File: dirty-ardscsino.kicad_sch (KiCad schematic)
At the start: 13 parts, among them J1 SCSI, J2 171825-4 (Ext. Power), J3 DM3AT-SF-PEJM5, U1 STM32 Bluepill

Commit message: Dirty ArdSCSIno 2 v1 sent to fab
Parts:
- removed JP2, JP3: Jumper_NC_Small, Connector_PinHeader_2.54mm:PinHeader_1x02_P2.54mm_Vertical, symbol Jumper:Jumper_2_Bridged
- added JP4, JP5: Jumper_2_Small_Bridged, Jumper:SolderJumper-2_P1.3mm_Bridged_RoundedPad1.0x1.5mm, symbol Jumper:Jumper_2_Small_Bridged
- added U2: microSD-Breakout, microSD_Breakout:microSD_AliExpress, symbol microSD_Breakout:microSD-Breakout
- C2: footprint Capacitor_SMD:C_0805_2012Metric_Pad1.15x1.40mm_HandSolder -> Capacitor_SMD:C_0805_2012Metric_Pad1.18x1.45mm_HandSolder
- JP1: value Jumper_NC_Small -> TERM_PWR_EN
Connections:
- net +5V: now also C2.2, RN1.1 (common), RN4.1 (common)
- net GND: now also C2.1, RN2.1 (common), RN3.1 (common), U2.6 (GND)
- net SD_CS: now also U2.2 (~{CS})
- net SD_CSK: now also U2.4 (CLK)
- net SD_MISO: now also JP5.2 (B), U2.5 (MISO); no longer U1.PA6
- net SD_MOSI: now also JP4.2 (B), U2.3 (MOSI); no longer U1.PA7
- net SD_VCC: now also U2.1 (3.3V)
- new net BP_MISO: JP5.1 (A), U1.PA6
- new net BP_MOSI: JP4.1 (A), U1.PA7
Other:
- note added: "Optional: use through-hole AliExpress breakout instead of proper surface-mount SD card slot"
- note added: "Preferred: use surface-mount microSD slot"
- moved on the sheet: J3

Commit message: Schem cleanup
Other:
- note removed: "TODO: Assign pins to SCSI connector, add SD card slot"
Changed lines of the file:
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@@
-		)
-	)
-	(text "TODO: Assign pins to SCSI connector, add SD card slot"
-		(exclude_from_sim no)
-		(at 118.11 73.025 90)
-		(effects
-			(font
-				(size 1.27 1.27)
-			)
-			(justify right bottom)
 		)
 	)
@@
 	(wire
 		(pts
-			(xy 31.115 167.005) (xy 34.29 167.005)
+			(xy 31.115 167.005) (xy 33.655 167.005)
 		)
 		(stroke
@@
 	)
 	(label "SD_MISO"
-		(at 34.29 167.005 0)
-		(effects
-			(font
+		(at 33.655 167.005 0)
+		(effects
+			(font

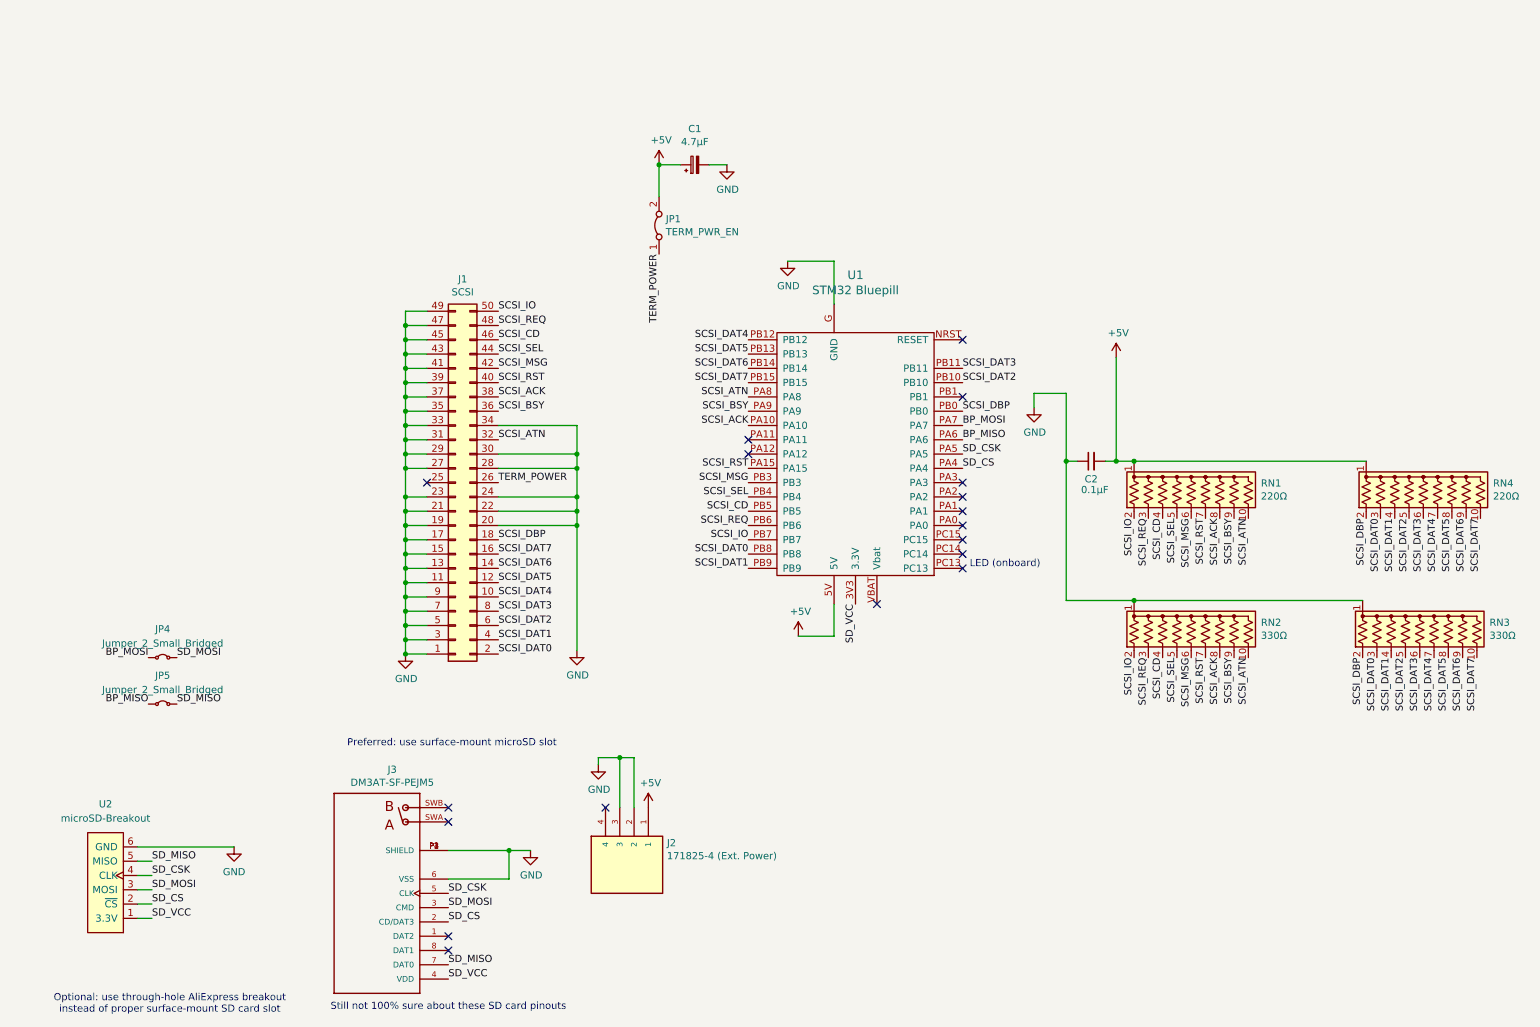
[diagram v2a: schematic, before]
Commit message: Remove MISO/MOSI poke-a-yoke; install termination-killing jumpers
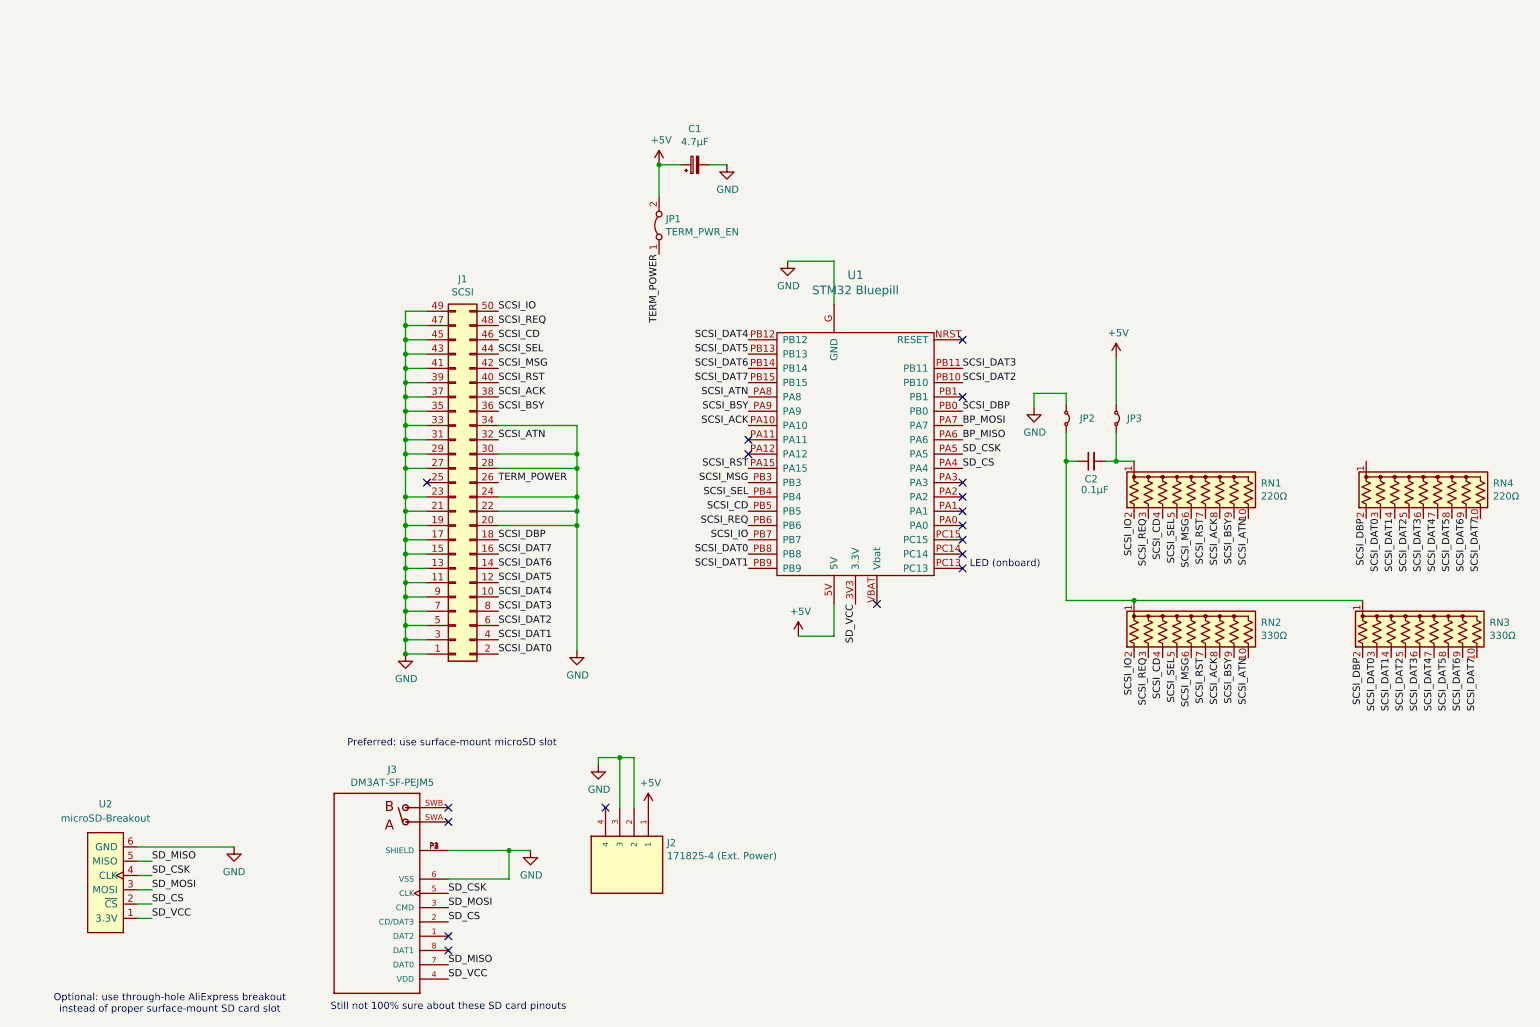
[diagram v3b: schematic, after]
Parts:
- removed JP4, JP5: Jumper_2_Small_Bridged, Jumper:SolderJumper-2_P1.3mm_Bridged_RoundedPad1.0x1.5mm, symbol Jumper:Jumper_2_Small_Bridged
- added JP2, JP3: Jumper_2_Small_Bridged, Jumper:SolderJumper-2_P1.3mm_Bridged_RoundedPad1.0x1.5mm, symbol Jumper:Jumper_2_Small_Bridged
- J2: footprint TE_171825-4 -> 171825-4:TE_171825-4
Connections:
- net +5V: now also JP3.1 (A); no longer C2.2, RN1.1 (common), RN4.1 (common)
- net GND: now also JP2.1 (A); no longer C2.1, RN2.1 (common), RN3.1 (common)
- new net: C2.2, JP3.2 (B), RN1.1 (common)
- new net: C2.1, JP2.2 (B), RN2.1 (common), RN3.1 (common)
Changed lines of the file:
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@@
 	)
 	(junction
-		(at 208.28 95.885)
-		(diameter 0)
-		(color 0 0 0 0)
-	)
-	(junction
 		(at 208.28 120.65)
 		(diameter 0)
@@
 	(wire
 		(pts
+			(xy 205.105 90.805) (xy 205.105 95.885)
+		)
+		(stroke
+			(width 0)
+			(type default)
+		)
+	)
+	(wire
+		(pts
 			(xy 82.55 69.215) (xy 78.74 69.215)
 		)
@@
 	(wire
 		(pts
+			(xy 196.215 90.805) (xy 196.215 95.885)
+		)
+		(stroke
+			(width 0)
+			(type default)
+		)
+	)
+	(wire
+		(pts
 			(xy 31.115 177.165) (xy 33.655 177.165)
 		)
@@
 	(wire
 		(pts
-			(xy 205.105 77.47) (xy 205.105 95.885)
+			(xy 205.105 77.47) (xy 205.105 85.725)
 		)
 		(stroke
@@
 	(wire
 		(pts
-			(xy 196.215 83.82) (xy 196.215 95.885)
+			(xy 196.215 83.82) (xy 196.215 85.725)
 		)
 		(stroke
@@
 	(wire
 		(pts
-			(xy 208.28 95.885) (xy 249.555 95.885)
-		)
-		(stroke
-			(width 0)
-			(type default)
-		)
-	)
-	(wire
-		(pts
 			(xy 208.28 120.65) (xy 248.92 120.65)
 		)
@@
 		)
 	)
-	(label "SD_MISO"
-		(at 38.1 139.065 0)
-		(effects
-			(font
-				(size 1.27 1.27)
-			)
-			(justify left bottom)
-		)
-	)
-	(label "SD_MOSI"
-		(at 38.1 130.81 0)
-		(effects
-			(font
-				(size 1.27 1.27)
-			)
-			(justify left bottom)
-		)
-	)
 	(label "SCSI_DAT3"
 		(at 177.8 79.375 0)
@@
 		)
 	)
-	(label "BP_MOSI"
-		(at 33.02 130.81 180)
-		(effects
-			(font
-				(size 1.27 1.27)
-			)
-			(justify right bottom)
-		)
-	)
 	(label "SD_CSK"
 		(at 86.36 172.72 0)
@@
 		)
 	)
-	(label "BP_MISO"
-		(at 33.02 139.065 180)
-		(effects
-			(font
-				(size 1.27 1.27)
-			)
-			(justify right bottom)
-		)
-	)
 	(label "SCSI_DAT0"
 		(at 252.095 106.045 270)
@@
 			)
 		)
-		(property "Footprint" "TE_171825-4"
+		(property "Footprint" "171825-4:TE_171825-4"
 			(at 116.84 167.64 0)
 			(effects
@@
 	)
 	(symbol
+		(lib_name "Jumper_2_Small_Bridged_1")
 		(lib_id "Jumper:Jumper_2_Small_Bridged")
-		(at 35.56 130.81 0)
+		(at 205.105 88.265 270)
 		(unit 1)
-		(exclude_from_sim yes)
+		(exclude_from_sim no)
 		(in_bom yes)
 		(on_board yes)
 		(dnp no)
 		(fields_autoplaced yes)
-		(property "Reference" "JP4"
-			(at 35.56 125.73 0)
+		(property "Reference" "JP3"
+			(at 207.01 88.2649 90)
 			(effects
 				(font
 					(size 1.27 1.27)
 				)
+				(justify left)
 			)
 		)
 		(property "Value" "Jumper_2_Small_Bridged"
-			(at 35.56 128.27 0)
+			(at 206.375 89.5349 90)
 			(effects
 				(font
 					(size 1.27 1.27)
 				)
+				(justify left)
+				(hide yes)
 			)
 		)
 		(property "Footprint" "Jumper:SolderJumper-2_P1.3mm_Bridged_RoundedPad1.0x1.5mm"
-			(at 35.56 130.81 0)
+			(at 205.105 88.265 0)
 			(effects
 				(font
@@
 		)
 		(property "Datasheet" "~"
-			(at 35.56 130.81 0)
+			(at 205.105 88.265 0)
 			(effects
 				(font
@@
 		)
 		(property "Description" "Jumper, 2-pole, small symbol, bridged"
-			(at 35.56 130.81 0)
-			(effects
-				(font
-					(size 1.27 1.27)
-				)
-				(hide yes)
-			)
-		)
-		(property "DigiKey" ""
-			(at 35.56 130.81 0)
+			(at 205.105 88.265 0)
 			(effects
 				(font
@@
 		)
 		(instances
-			(project ""
+			(project "dirty-ardscsino"
 				(path "/104d678f-d12a-483d-a1a0-89cafc11d4bb"
-					(reference "JP4")
+					(reference "JP3")
 					(unit 1)
 				)
@@
 	)
 	(symbol
-		(lib_id "Jumper:Jumper_2_Small_Bridged")
-		(at 35.56 139.065 0)
+		(lib_name "GND_1")
+		(lib_id "power:GND")
+		(at 48.26 164.465 0)
 		(unit 1)
-		(exclude_from_sim yes)
+		(exclude_from_sim no)
 		(in_bom yes)
 		(on_board yes)
 		(dnp no)
-		(fields_autoplaced yes)
-		(property "Reference" "JP5"
-			(at 35.56 133.985 0)
-			(effects
-				(font
-					(size 1.27 1.27)
-				)
-			)
-		)
-		(property "Value" "Jumper_2_Small_Bridged"
-			(at 35.56 136.525 0)
+		(property "Reference" "#PWR01"
+			(at 48.26 170.815 0)
 			(effects
 				(font
 					(size 1.27 1.27)
 				)
+				(hide yes)
 			)
 		)
-		(property "Footprint" "Jumper:SolderJumper-2_P1.3mm_Bridged_RoundedPad1.0x1.5mm"
-			(at 35.56 139.065 0)
+		(property "Value" "GND"
+			(at 48.26 168.91 0)
 			(effects
 				(font
 					(size 1.27 1.27)
 				)
-				(hide yes)
 			)
 		)
-		(property "Datasheet" "~"
-			(at 35.56 139.065 0)
+		(property "Footprint" ""
+			(at 48.26 164.465 0)
 			(effects
 				(font
@@
 			)
 		)
-		(property "Description" "Jumper, 2-pole, small symbol, bridged"
-			(at 35.56 139.065 0)
+		(property "Datasheet" ""
+			(at 48.26 164.465 0)
 			(effects
 				(font
@@
 			)
 		)
-		(property "DigiKey" ""
-			(at 35.56 139.065 0)
+		(property "Description" "Power symbol creates a global label with name \"GND\" , ground"
+			(at 48.26 164.465 0)
 			(effects
 				(font
@@
 		(pin "1"
 		)
-		(pin "2"
-		)
 		(instances
-			(project "dirty-ardscsino"
+			(project ""
 				(path "/104d678f-d12a-483d-a1a0-89cafc11d4bb"
-					(reference "JP5")
+					(reference "#PWR01")
 					(unit 1)
 				)
@@
 	)
 	(symbol
-		(lib_name "GND_1")
-		(lib_id "power:GND")
-		(at 48.26 164.465 0)
+		(lib_name "Jumper_2_Small_Bridged_1")
+		(lib_id "Jumper:Jumper_2_Small_Bridged")
+		(at 196.215 88.265 270)
 		(unit 1)
 		(exclude_from_sim no)
@@
 		(on_board yes)
 		(dnp no)
-		(property "Reference" "#PWR01"
-			(at 48.26 170.815 0)
+		(property "Reference" "JP2"
+			(at 201.295 88.265 90)
 			(effects
 				(font
 					(size 1.27 1.27)
 				)
-				(hide yes)
+				(justify right)
 			)
 		)
-		(property "Value" "GND"
-			(at 48.26 168.91 0)
+		(property "Value" "Jumper_2_Small_Bridged"
+			(at 194.31 86.9951 90)
 			(effects
 				(font
 					(size 1.27 1.27)
 				)
+				(justify right)
+				(hide yes)
 			)
 		)
-		(property "Footprint" ""
-			(at 48.26 164.465 0)
+		(property "Footprint" "Jumper:SolderJumper-2_P1.3mm_Bridged_RoundedPad1.0x1.5mm"
+			(at 196.215 88.265 0)
 			(effects
 				(font
@@
 			)
 		)
-		(property "Datasheet" ""
-			(at 48.26 164.465 0)
+		(property "Datasheet" "~"
+			(at 196.215 88.265 0)
 			(effects
 				(font
@@
 			)
 		)
-		(property "Description" "Power symbol creates a global label with name \"GND\" , ground"
-			(at 48.26 164.465 0)
+		(property "Description" "Jumper, 2-pole, small symbol, bridged"
+			(at 196.215 88.265 0)
 			(effects
 				(font
@@
 		(pin "1"
 		)
+		(pin "2"
+		)
 		(instances
 			(project ""
 				(path "/104d678f-d12a-483d-a1a0-89cafc11d4bb"
-					(reference "#PWR01")
+					(reference "JP2")
 					(unit 1)
 				)

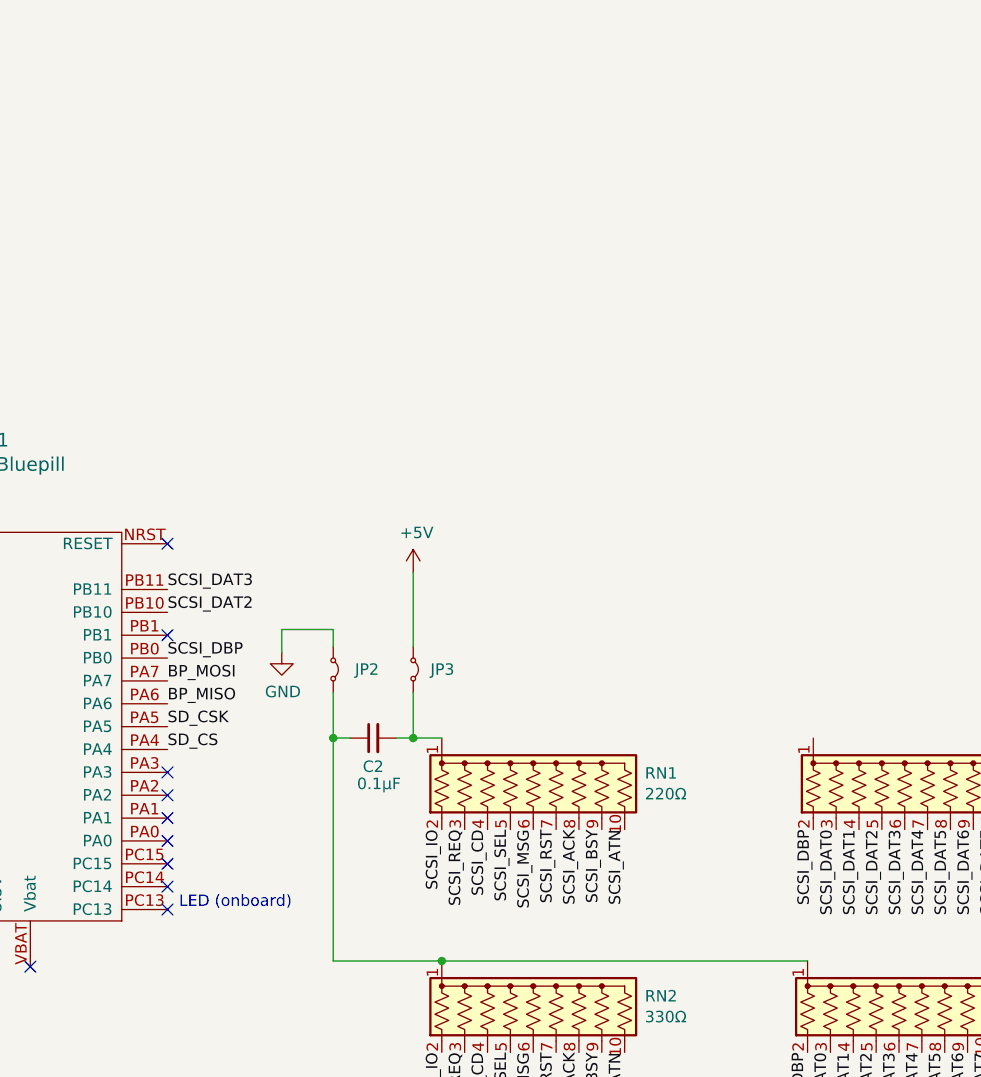
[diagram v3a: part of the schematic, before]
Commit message: Optional activity LED
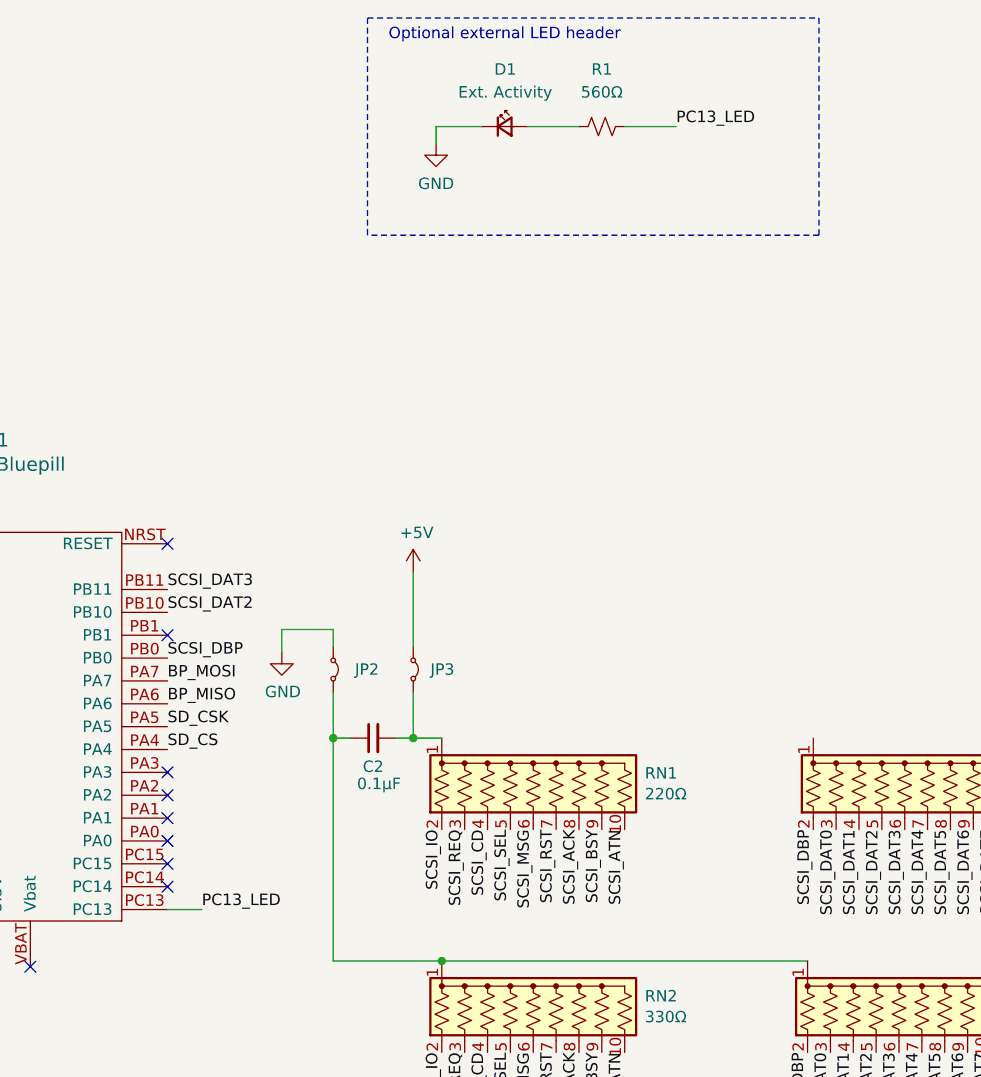
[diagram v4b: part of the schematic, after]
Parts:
- added D1: Ext. Activity, LED_THT:LED_D3.0mm, symbol Device:LED_Small
- added R1: 560Ω, Resistor_THT:R_Axial_DIN0207_L6.3mm_D2.5mm_P10.16mm_Horizontal, symbol Device:R_Small_US
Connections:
- net GND: now also D1.1 (K)
- net PC13_LED: now reaches U1.PC13
- net PC13_LED: now also R1.2
- new net: D1.2 (A), R1.1
- no-connect marks 18 -> 17
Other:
- note added: "Optional external LED header"
- note removed: "LED (onboard)"

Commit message: Add LCSC part for the SD card
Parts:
- J3: LCSC (none) -> C114218
- JP1, JP2, JP3: now left out of the parts list
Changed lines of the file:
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@@
 		(unit 1)
 		(exclude_from_sim no)
-		(in_bom yes)
+		(in_bom no)
 		(on_board yes)
 		(dnp no)
@@
 					(size 1.27 1.27)
 				)
+			)
+		)
+		(property "DigiKey" ""
+			(at 123.825 53.975 0)
+			(effects
+				(font
+					(size 1.27 1.27)
+				)
+				(hide yes)
 			)
 		)
@@
 			)
 		)
+		(property "LCSC" ""
+			(at 200.66 95.885 90)
+			(effects
+				(font
+					(size 1.27 1.27)
+				)
+				(hide yes)
+			)
+		)
 		(pin "1"
 		)
@@
 		)
 		(property "DigiKey" "HR1964CT-ND"
+			(at 73.66 172.72 0)
+			(effects
+				(font
+					(size 1.27 1.27)
+				)
+				(hide yes)
+			)
+		)
+		(property "LCSC" "C114218"
 			(at 73.66 172.72 0)
 			(effects
@@
 		(unit 1)
 		(exclude_from_sim no)
-		(in_bom yes)
+		(in_bom no)
 		(on_board yes)
 		(dnp no)
@@
 			)
 		)
+		(property "DigiKey" ""
+			(at 205.105 88.265 0)
+			(effects
+				(font
+					(size 1.27 1.27)
+				)
+				(hide yes)
+			)
+		)
 		(pin "1"
 		)
@@
 		(unit 1)
 		(exclude_from_sim no)
-		(in_bom yes)
+		(in_bom no)
 		(on_board yes)
 		(dnp no)
@@
 			(at 196.215 88.265 0)
 			(effects
+				(font
+					(size 1.27 1.27)
+				)
+				(hide yes)
+			)
+		)
+		(property "DigiKey" ""
+			(at 196.215 88.265 0)
+			(effects

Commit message: Fix potential bug, BOM
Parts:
- J2: DigiKey A106197-NDr -> A106197-ND
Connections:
- net at C2.2, JP3.2 (B), RN1.1 (common): now also RN4.1 (common)
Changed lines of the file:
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@@
 	)
 	(junction
+		(at 208.28 95.885)
+		(diameter 0)
+		(color 0 0 0 0)
+	)
+	(junction
 		(at 78.74 107.315)
 		(diameter 0)
@@
 	(wire
 		(pts
+			(xy 208.28 95.885) (xy 249.555 95.885)
+		)
+		(stroke
+			(width 0)
+			(type default)
+		)
+	)
+	(wire
+		(pts
 			(xy 109.22 104.775) (xy 109.22 102.235)
 		)
@@
 			)
 		)
-		(property "DigiKey" "A106197-ND\r"
+		(property "DigiKey" "A106197-ND"
 			(at 116.84 167.64 90)
 			(effects
